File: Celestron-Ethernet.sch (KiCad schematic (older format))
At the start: 73 parts, among them J1 FTDI, J2 RJ45_Amphenol_RJMG1BD3B8K1ANR, J3 6P6C, SW1 SW_Push, SW2 SW_DIP_x02, U1 W5500, U2 ATmega328P-AU, U3 LP2985-3.3, U4 LP2985-5.0, Y1 16MHz, Y2 25MHz

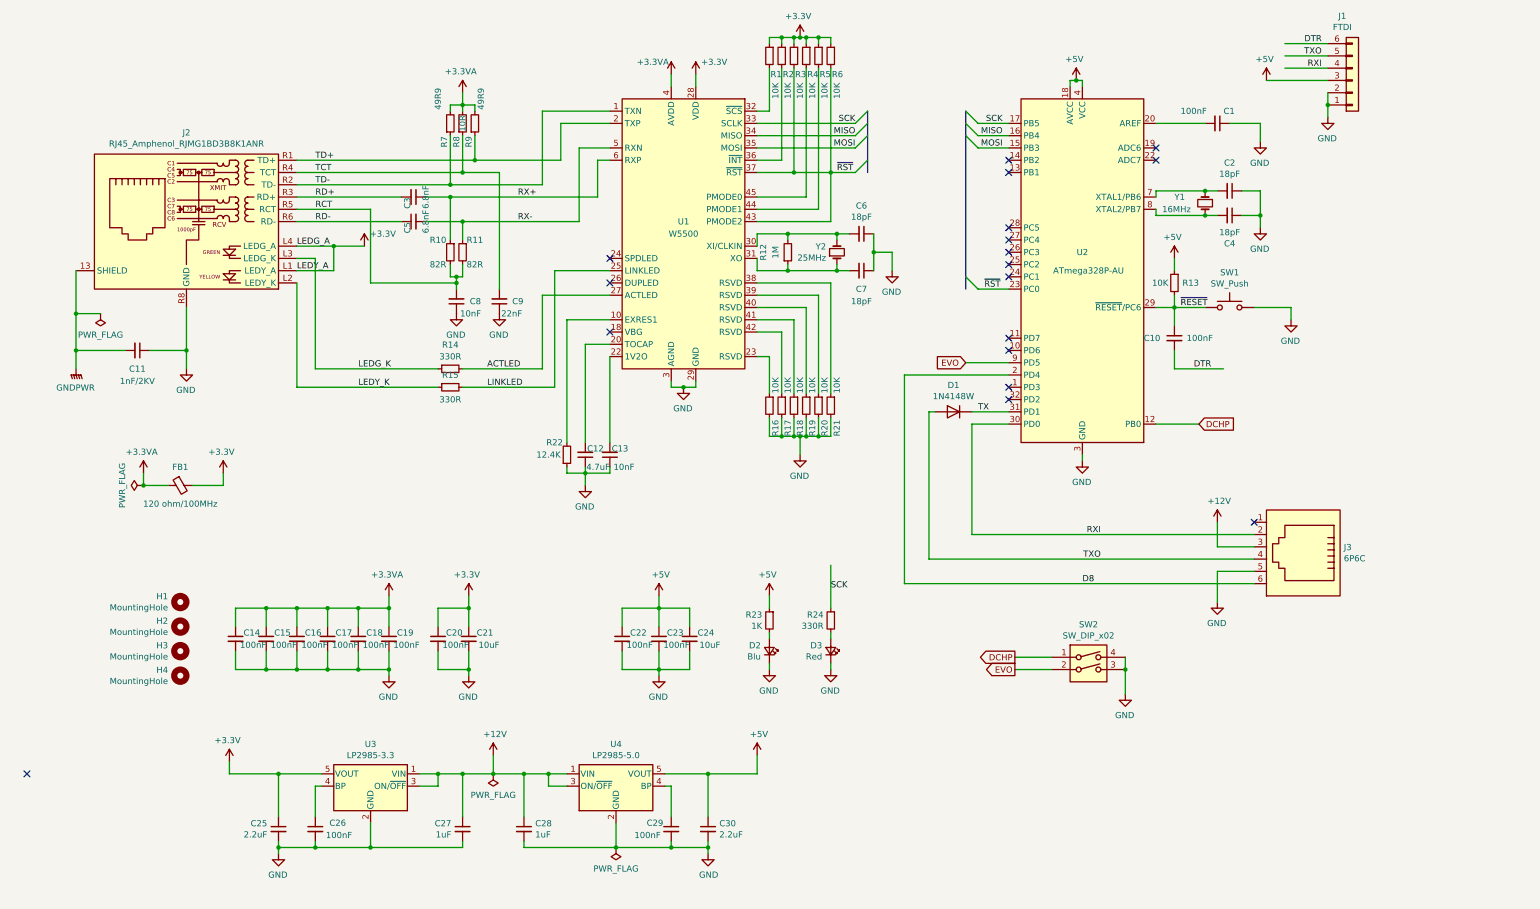
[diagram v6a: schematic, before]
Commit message: Added aux port pullups
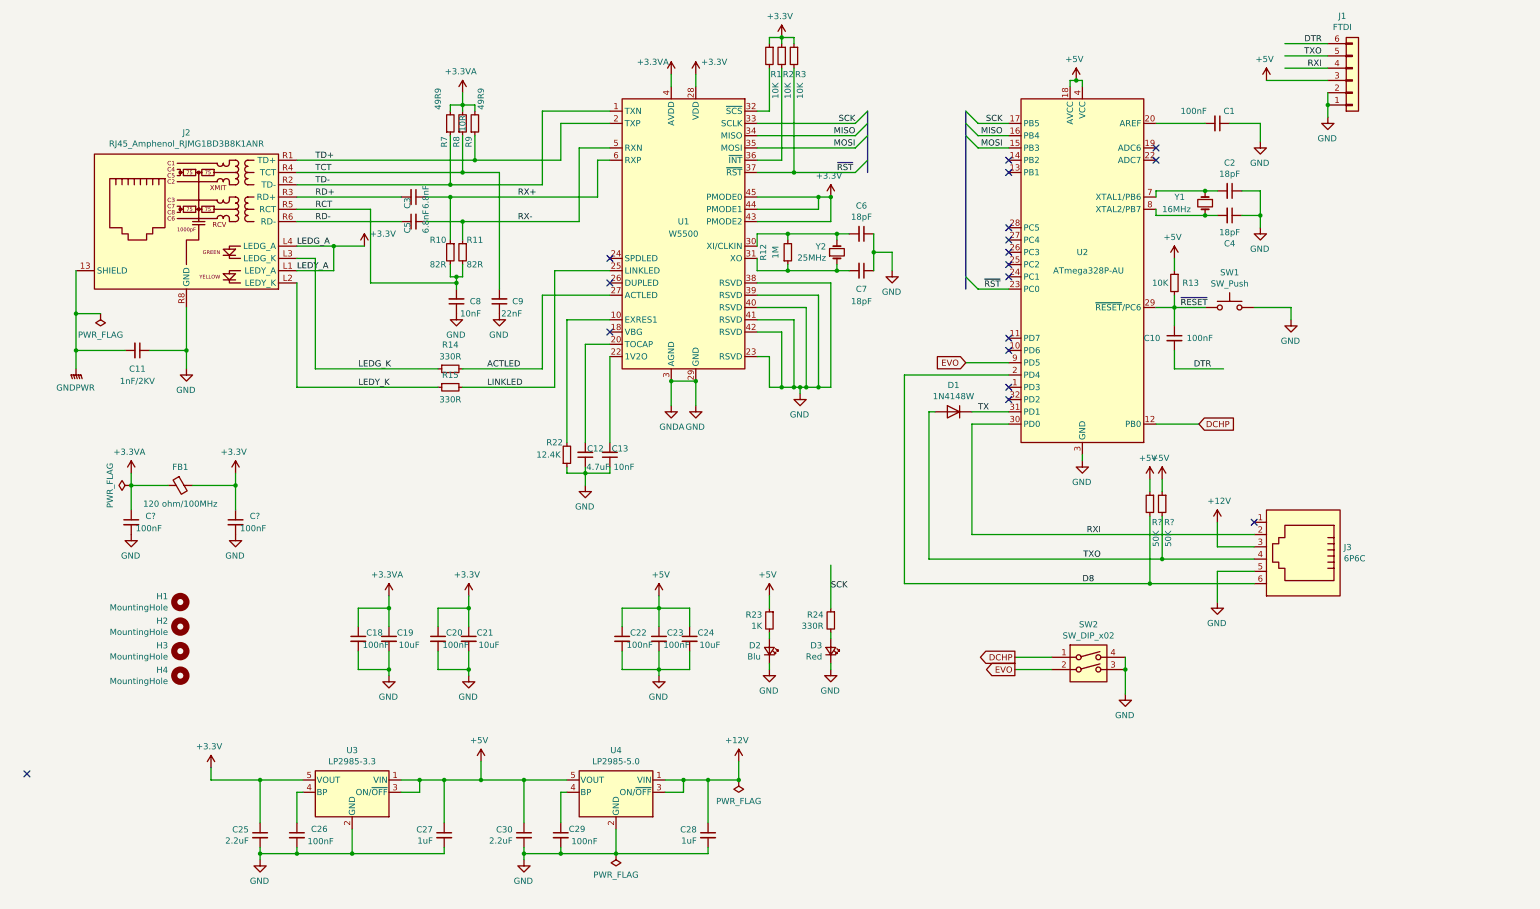
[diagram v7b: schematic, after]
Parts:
- removed C14, C15, C16, C17: 100nF, Capacitor_SMD:C_0603_1608Metric, symbol Device:C_Small
- removed R16, R17, R18, R19, R20, R21, R4, R5, R6: 10K, Resistor_SMD:R_0603_1608Metric, symbol Device:R_Small
- added C? (x2): 100nF, Capacitor_SMD:C_0603_1608Metric, symbol Device:C_Small
- added R? (x2): 50K, Resistor_SMD:R_0603_1608Metric, symbol Device:R_Small
- C19: value 100nF -> 10uF
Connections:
- net +12V: no longer C27.1, U3.1 (VIN), U3.3 (ON/~OFF~)
- net +3.3VA: now also C?.1
- net +3V3: now also U1.43 (PMODE2), U1.44 (PMODE1), U1.45 (PMODE0), C?.1
- net +5V: now also C27.1, U3.1 (VIN), U3.3 (ON/~OFF~), R?.1, R?.1
- net D8: now also R?.2
- net GND: now also U1.23 (RSVD), U1.38 (RSVD), U1.39 (RSVD), U1.40 (RSVD), U1.41 (RSVD), U1.42 (RSVD), C?.2, C?.2
- net TXO: now also R?.2
- net ~RST: no longer U1.43 (PMODE2)
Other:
- moved on the sheet: C25, C26, C27, C28, C29, C30, U3, U4

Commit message: 3v3 version
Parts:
- removed C26, C29: 100nF, Capacitor_SMD:C_0603_1608Metric, symbol Device:C_Small
- removed C28: 1uF, Capacitor_SMD:C_0603_1608Metric, symbol Device:C_Small
- removed C30: 2.2uF, Capacitor_SMD:C_0603_1608Metric, symbol Device:C_Small
- removed D3: Red, LED_SMD:LED_0603_1608Metric, symbol Device:LED_Small
- removed R24: 330R, Resistor_SMD:R_0603_1608Metric, symbol Device:R_Small
- removed U3: LP2985-3.3, Package_TO_SOT_SMD:SOT-23-5, symbol Regulator_Linear:LP2985-3.3
- removed U4: LP2985-5.0, Package_TO_SOT_SMD:SOT-23-5, symbol Regulator_Linear:LP2985-5.0
- added D2: Grn, LED_SMD:LED_0603_1608Metric, symbol Device:LED_Small
- added R16: 330R, Resistor_SMD:R_0603_1608Metric, symbol Device:R_Small
- added U3: 74AHC1G125, Package_TO_SOT_SMD:SOT-23-5, symbol 74xGxx:74AHC1G125
- added U4: NCV33375ST-3.3, Package_TO_SOT_SMD:SOT-223, symbol Regulator_Linear:NCV33375ST-3.3
- C24: renamed from C25; value 2.2uF -> 1uF
- D3: renamed from D2; value Blu -> Red
- R17: renamed from R23; value 1K -> 330R
- Y1: value 16MHz -> 8MHz
- gave numbers to parts that had none: 4
- renumbered C18 to C16, C19 to C17, C20 to C18, C21 to C19, C22 to C20, C23 to C21, C24 to C22, C27 to C23, R13 to R10, R14 to R11, R15 to R12, R22 to R13, R7 to R4, R8 to R5, R9 to R6, R10 to R7, R11 to R8, R12 to R9
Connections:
- net +12V: now also C23.1, U4.1 (IN), U4.2 (EN)
- net GND: now also U3.1, U3.3 (GND), U4.4 (GND)
- net SCK: now also U3.2
- net +3V3 renamed VCC
- net VCC: now also C20.1, C21.1, C22.1, J1.3 (Pin_3), R10.1, R14.1, R15.1, R17.1, U2.18 (AVCC), U2.4 (VCC), U2.6 (VCC), R16.2, U3.5 (VCC), U4.3 (OUT)
- removed net +5V: C20.1, C21.1, C22.1, C23.1, J1.3 (Pin_3), R10.1, R14.1, R15.1, R17.1, U2.18 (AVCC), U2.4 (VCC), U2.6 (VCC)
- new net: D2.2 (A), R16.1
- new net: D2.1 (K), U3.4
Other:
- moved on the sheet: C20, C21, C22, C23, C24, D3, R14, R15, R17
